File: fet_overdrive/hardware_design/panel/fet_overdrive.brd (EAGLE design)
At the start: 30 x 128.5 mm, 1 part

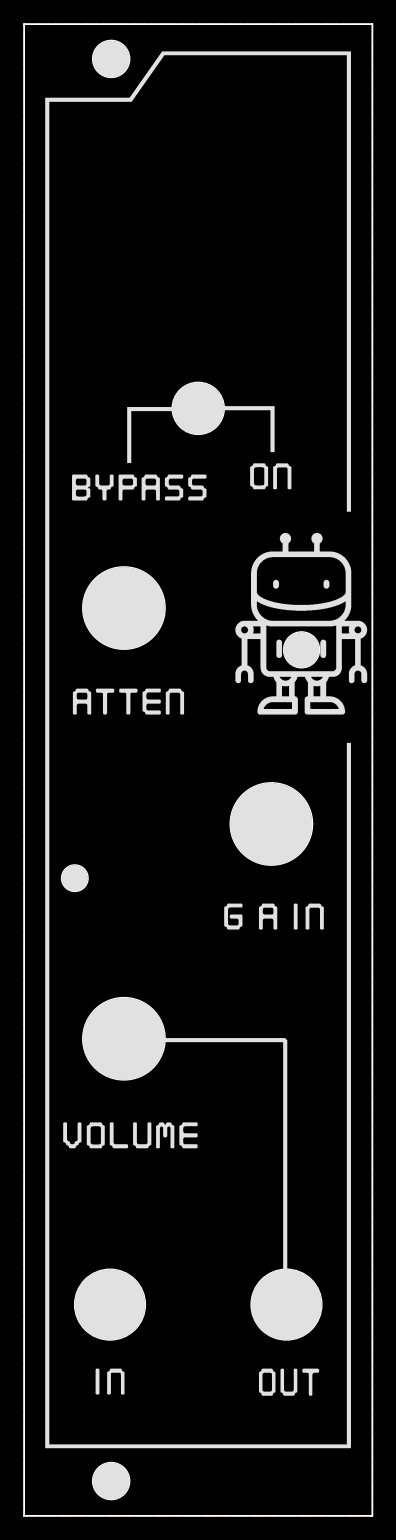
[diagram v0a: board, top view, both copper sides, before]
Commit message: design for fet overdrive and quantizer 2 code updates
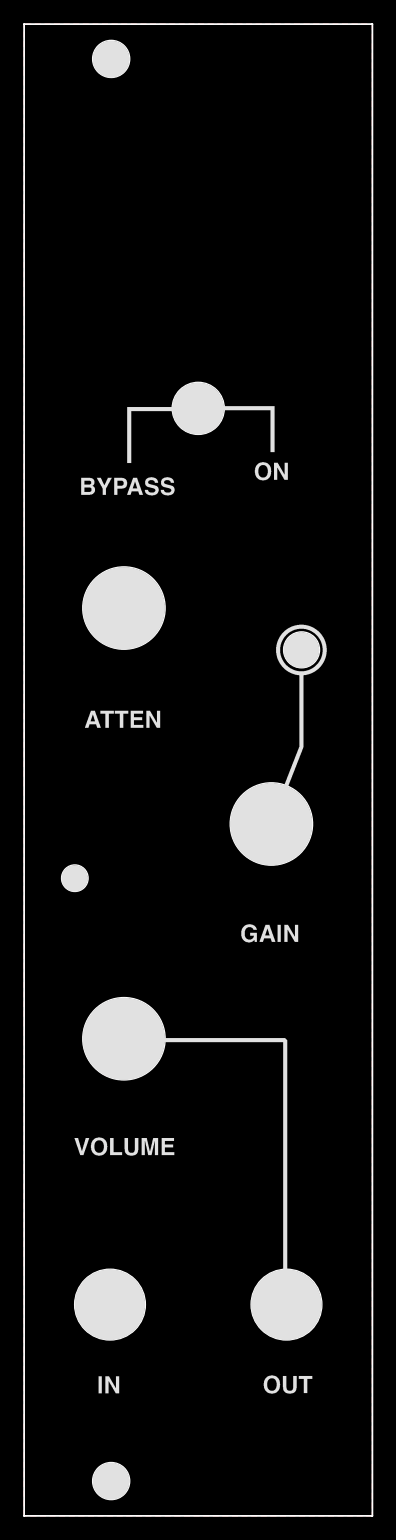
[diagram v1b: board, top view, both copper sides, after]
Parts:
- added E$2: (no value), Graphics v30:FET-SILK
- E$1: device Graphics v26:FET-OVERDRIVE-FUTURISTIC -> Graphics v30:FET-COPPER
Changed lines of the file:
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@@
 </autorouter>
 <elements>
-<element name="E$1" library="Graphics v26" package="FET-OVERDRIVE-FUTURISTIC" value="" x="0" y="0" smashed="yes"/>
+<element name="E$1" library="Graphics v30" package="FET-COPPER" value="" x="0" y="0" smashed="yes"/>
+<element name="E$2" library="Graphics v30" package="FET-SILK" value="" x="0" y="0" smashed="yes"/>
 </elements>
 <signals>
